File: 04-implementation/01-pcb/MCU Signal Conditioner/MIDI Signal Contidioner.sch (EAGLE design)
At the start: 26 parts, among them J2 ARDUINO-CONN-8X2, J3 ARDUINO-CONN-8X2, U4 24CS01, U6 MCP1700-SOT89, X1 SSW-107-02-S-D, X2 SSW-107-02-S-D, X3 SSW-107-02-S-D, X4 SSW-107-02-S-D, X5 MINI-USB-SHIELD-32005-201

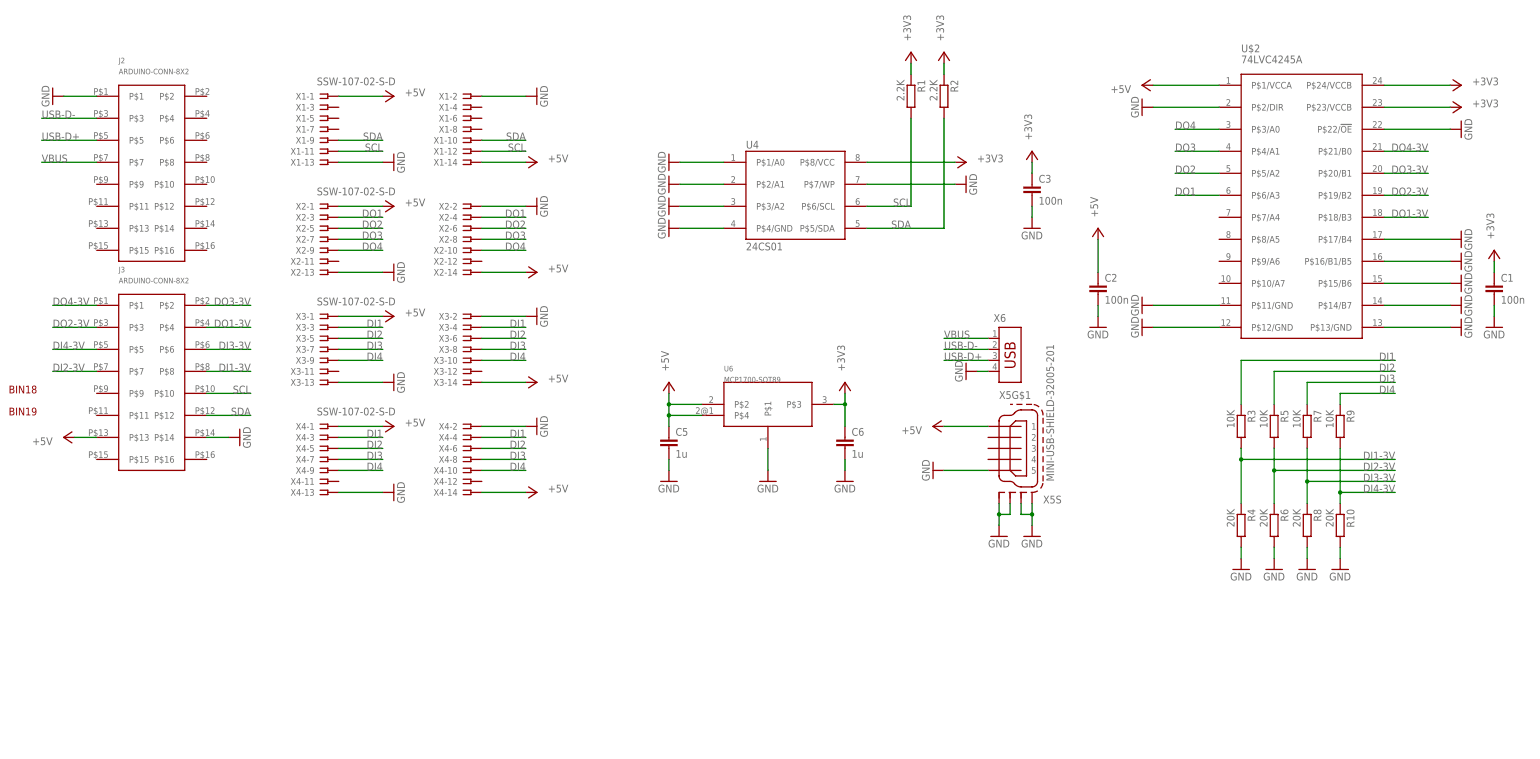
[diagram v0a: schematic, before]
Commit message: Add files for PCB releases.
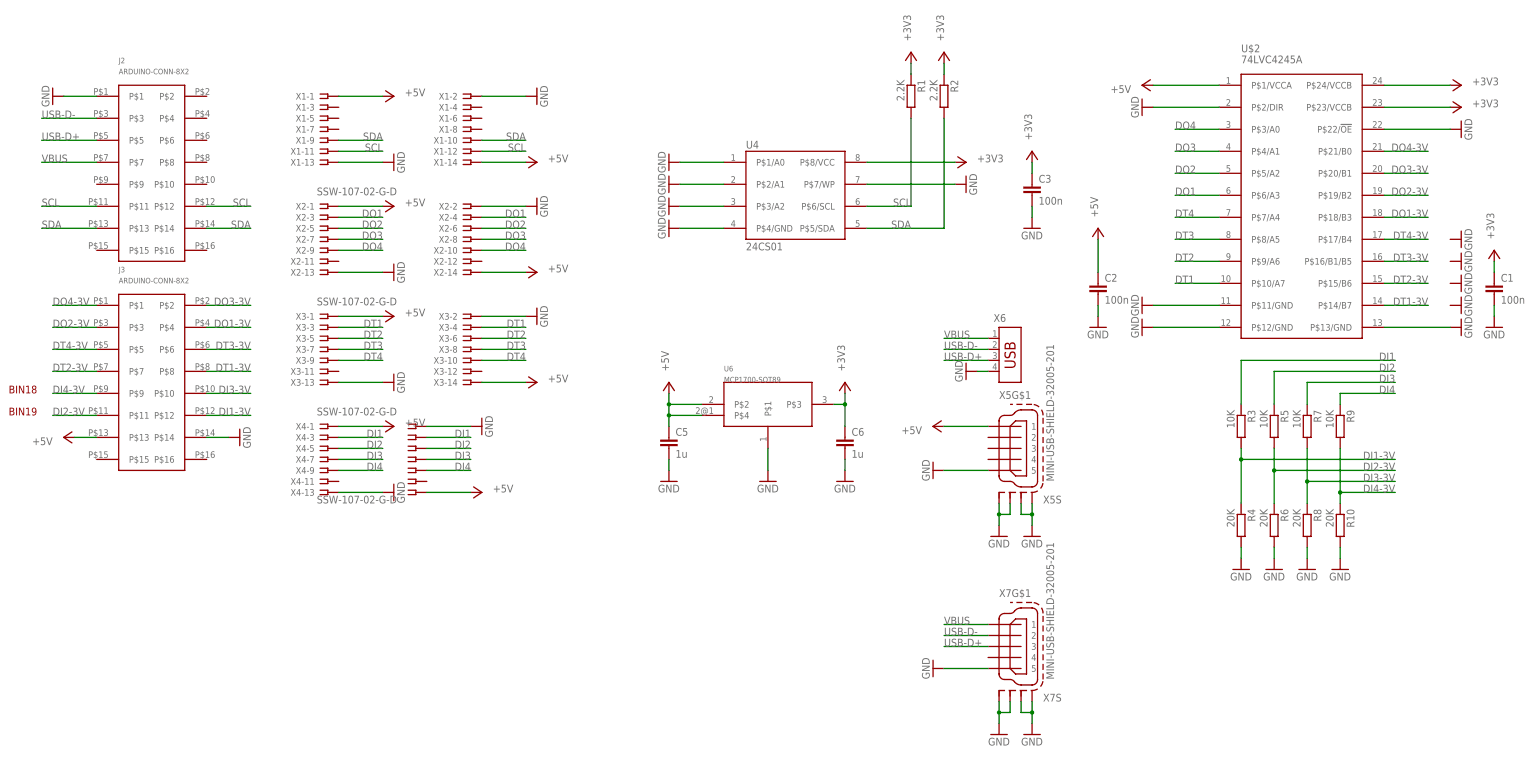
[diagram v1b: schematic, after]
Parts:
- added X7: MINI-USB-SHIELD-32005-201, MIDI router parts:MINI-USB-SHIELD-32005-201
- U$2: device MIDI Signal Conditioner Parts:74LVC4245A -> MIDI router parts:74LVC4245A
- U6: device MIDI Signal Conditioner Parts:MCP1700-SOT89 -> MIDI router parts:MCP1700-SOT89
- X1, X2, X3, X4: value SSW-107-02-S-D -> SSW-107-02-G-D; device con-samtec:SSW-107-02-S-D -> MIDI router parts:SSW-107-02-G-D
- X5: device MIDI Signal Conditioner Parts:MINI-USB-SHIELD-32005-201 -> MIDI router parts:MINI-USB-SHIELD-32005-201
- X6: device MIDI Signal Conditioner Parts:USB-787616 -> MIDI router parts:USB-787616
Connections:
- new net DT1: U$2.P$10/A7, X3-3.1, X3-4.1
- new net DT1-3V: J3.P$8, U$2.P$14/B7
- new net DT2: U$2.P$9/A6, X3-5.1, X3-6.1
- new net DT2-3V: J3.P$7, U$2.P$15/B6
- new net DT3: U$2.P$8/A5, X3-7.1, X3-8.1
- new net DT3-3V: J3.P$6, U$2.P$16/B1/B5
- new net DT4: U$2.P$7/A4, X3-10.1, X3-9.1
- new net DT4-3V: J3.P$5, U$2.P$17/B4
- net DI1: no longer X3-3.1, X3-4.1
- net DI1-3V: now also J3.P$12; no longer J3.P$8
- net DI2: no longer X3-5.1, X3-6.1
- net DI2-3V: now also J3.P$11; no longer J3.P$7
- net DI3: no longer X3-7.1, X3-8.1
- net DI3-3V: now also J3.P$10; no longer J3.P$6
- net DI4: no longer X3-10.1, X3-9.1
- net DI4-3V: now also J3.P$9; no longer J3.P$5
- net GND: now also X7G$1.5, X7S.S1, X7S.S2, X7S.S3, X7S.S4; no longer U$2.P$14/B7, U$2.P$15/B6, U$2.P$16/B1/B5, U$2.P$17/B4
- net SCL: now also J2.P$11, J2.P$12; no longer J3.P$10
- net SDA: now also J2.P$13, J2.P$14; no longer J3.P$12
- net USB-D+: now also X7G$1.3
- net USB-D-: now also X7G$1.2
- net VBUS: now also X7G$1.1
